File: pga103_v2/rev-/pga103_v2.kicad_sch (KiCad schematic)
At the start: 30 parts, among them J1 RF_IN, J2 RF_OUT, U1 SPX3819M5-L-5-0, U2 PGA-103, U3 RBP-XXX

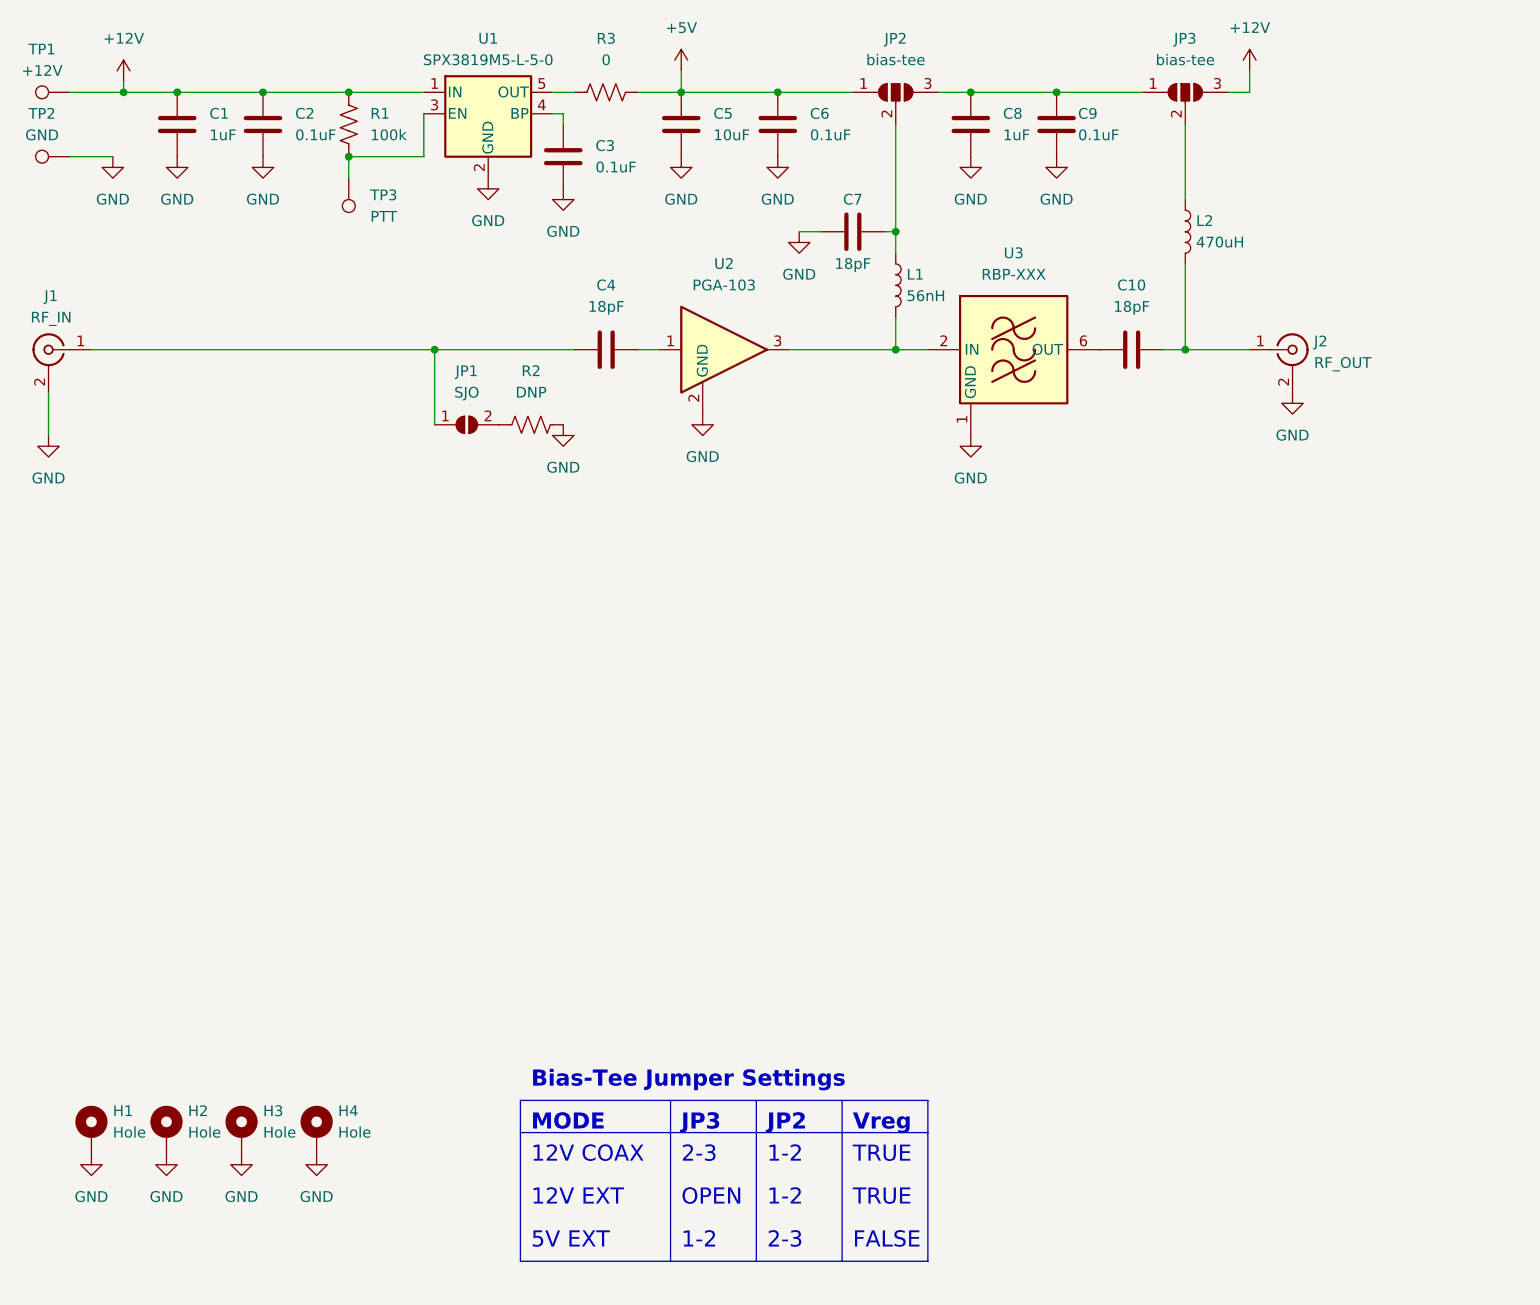
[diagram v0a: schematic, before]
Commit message: aded gitignore, about to rearrange for MAJOR.MINOR.PATCH versioning
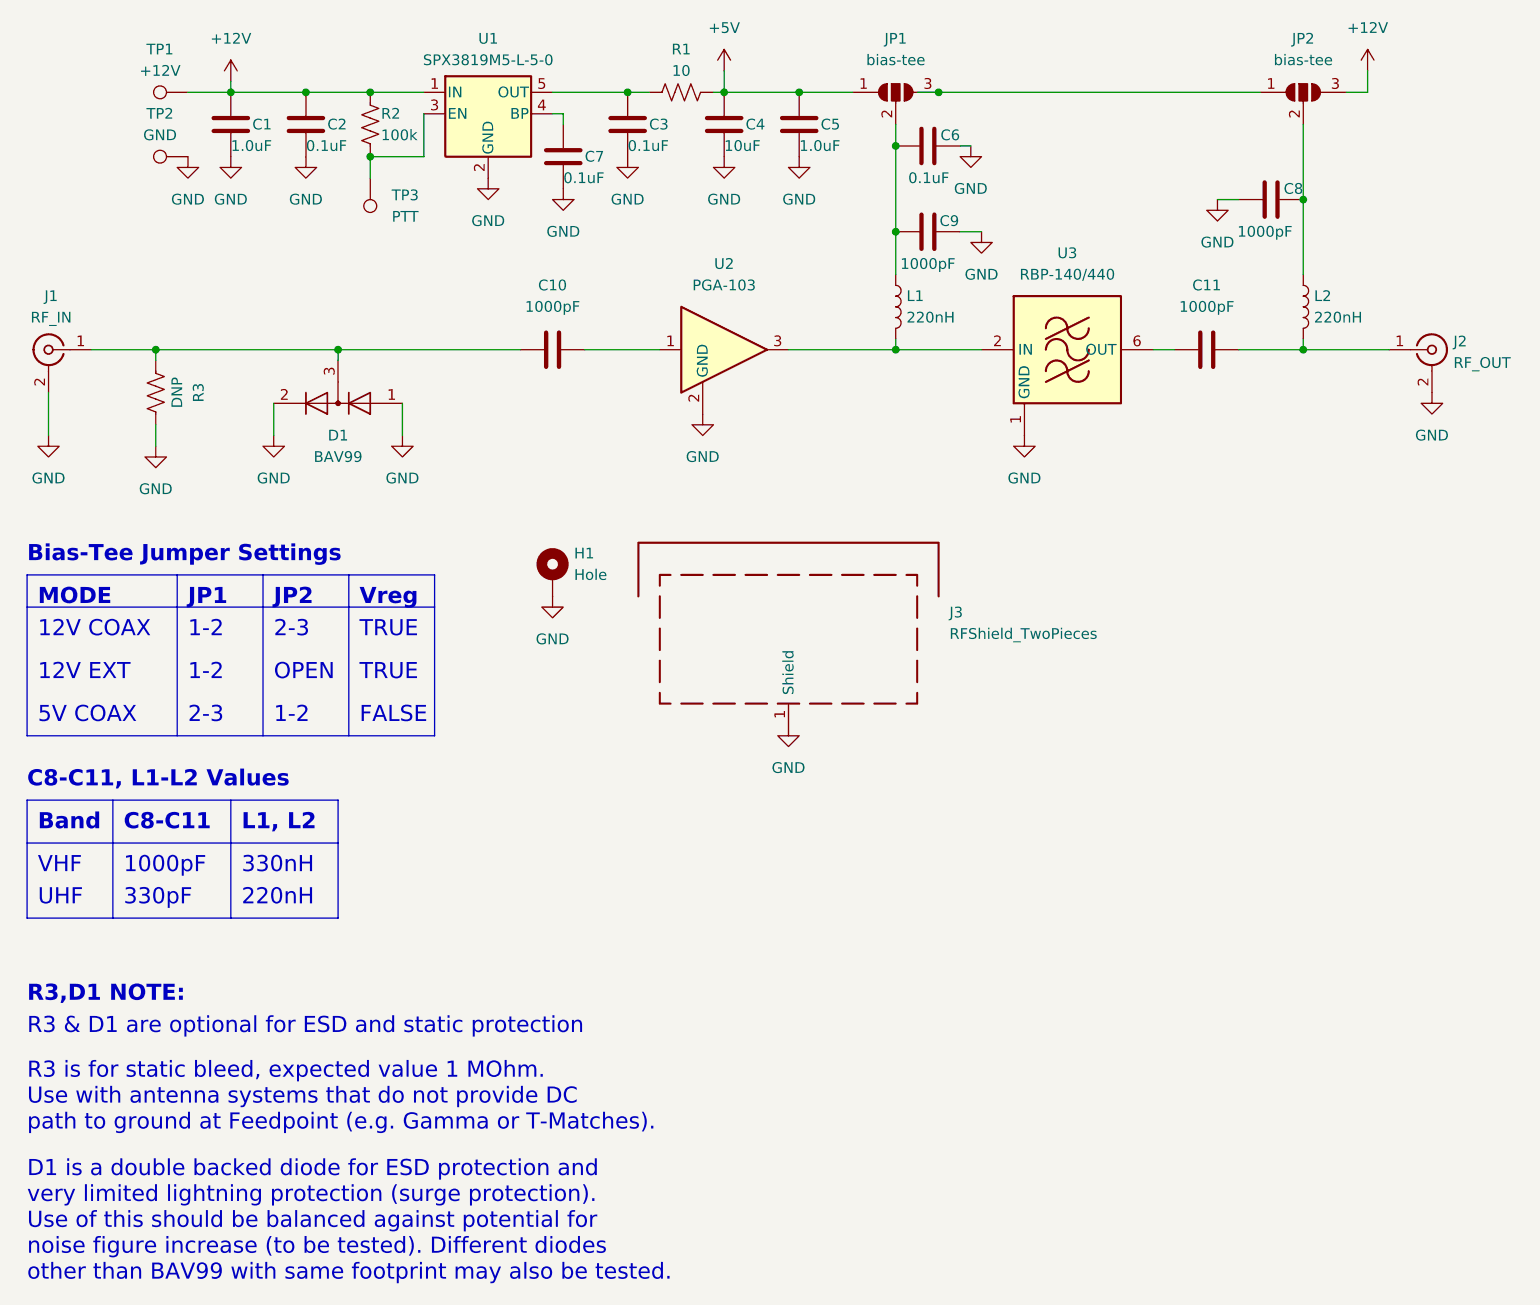
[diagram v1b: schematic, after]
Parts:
- removed H2, H3, H4: Hole, MountingHole:MountingHole_2.5mm_Pad_Via, symbol Mechanical:MountingHole_Pad
- removed JP1: SJO, Jumper:SolderJumper-2_P1.3mm_Open_RoundedPad1.0x1.5mm, symbol Jumper:SolderJumper_2_Open
- added C3: 0.1uF, digikey-footprints:0805, symbol Device:C
- added D1: BAV99, Package_TO_SOT_SMD:SOT-23, symbol Diode:BAV99
- added J3: RFShield_TwoPieces, RF_Shielding:Wuerth_36103205_20x20mm, symbol Device:RFShield_TwoPieces
- C1: value 1uF -> 1.0uF
- C10: renamed from C4; value 18pF -> 1000pF
- C11: renamed from C10; value 18pF -> 1000pF
- C5: renamed from C6; value 0.1uF -> 1.0uF
- C8: value 1uF -> 1000pF
- C9: renamed from C7; value 18pF -> 1000pF
- H1: footprint MountingHole:MountingHole_2.5mm_Pad_Via -> TestPoint:TestPoint_Plated_Hole_D4.0mm
- L1: value 56nH -> 220nH
- L2: value 470uH -> 220nH
- R1: renamed from R3; value 0 -> 10
- U3: value RBP-XXX -> RBP-140/440
- renumbered C5 to C4, C9 to C6, C3 to C7, JP2 to JP1, JP3 to JP2, R1 to R2, R2 to R3
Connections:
- net GND: now also C8.2, C3.1, D1.1 (K), D1.2 (A), J3.1 (Shield); no longer C8.1
- net at C9.2, JP1.2 (C), L1.1: now also C6.2
- net at C10.1, J1.1 (In): now also R3.1, D1.3 (K)
- net at JP2.2 (C), L2.1: now also C8.1
- net at R1.1, U1.5 (OUT): now also C3.2
- net at JP1.3 (B), JP2.1 (A): no longer C6.2, C8.2
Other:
- note added: "1000pF"
- note added: "220nH"
- note added: "330nH"
- note added: "330pF"
- note added: "5V COAX"
- note added: "Band"
- note added: "C8-C11"
- note added: "C8-C11, L1-L2 Values"
- note added: "D1 is a double backed diode for ESD protection and very limited lightning protection (surge protection). Use of this should be balanced against potential for noise figure increase (to be tested). Different diodes other than BAV99 with same footprint may also be tested."
- note added: "JP1"
- note added: "L1, L2"
- note added: "R3 & D1 are optional for ESD and static protection"
- note added: "R3 is for static bleed, expected value 1 MOhm. Use with antenna systems that do not provide DC path to ground at Feedpoint (e.g. Gamma or T-Matches)."
- note added: "R3,D1 NOTE:"
- note added: "UHF"
- note added: "VHF"
- note removed: "5V EXT"
- note removed: "JP3"
- title: PGA-103+ Preamplifier, Version 2 -> PGA-103+ Preamplifier, Version 1
- moved on the sheet: C1, C10, C11, C2, C4, C5, C6, C8, C9, H1, J2, JP2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
